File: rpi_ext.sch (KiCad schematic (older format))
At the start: 4 parts, among them J2 USB_OTG

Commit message: update pdf
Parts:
- added C11, C12, C7, C8: 10uF, symbol C_Small
- added C2: 47uF, symbol C_Small
- added C21, C22: NF, symbol C_Small
- added C6: 100nF, symbol C_Small
- added L1, L2: SRN4018-4R7M, symbol L_Small
- added PP2, PP3, PP5, PP6, PP8: TEST_1P, symbol TEST_1P
- added R2: 100K/1%, symbol R_Small
- added R22, R23: 0R/1%, symbol R_Small
- added R24, R25: 0R, symbol R_Small
- added U?: PAM2306AYPKE, symbol PAM2306AYPKE
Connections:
- net at J2.1 (VCC): now also F1.1, PP1.1
- net GND: now reaches J2.5 (GND)
- net GND: now also J2.6 (shield), C11.2, C12.2, C2.2, C6.2, C7.2, C8.2, PP5.1, PP8.1, R24.2, R25.2, U?.13 (PAD), U?.3 (GND), U?.9 (GND)
- net +5V: now reaches F1.2
- net +5V: now also C2.1, C7.1, C8.1, PP3.1, R2.1, U?.1 (VIN2), U?.6 (EN1), U?.7 (VIN1)
- new net: C22.2, R23.2, R24.1, U?.10 (FB2)
- new net: C6.1, R2.2, U?.12 (EN2)
- new net: L2.1, U?.2 (LX2)
- new net: C21.2, R22.2, R25.1, U?.4 (FB1)
- new net: L1.1, U?.8 (LX1)
- new net +1V8: C12.1, C22.1, L2.2, PP6.1, R23.1
- new net +3V3: C11.1, C21.1, L1.2, PP2.1, R22.1
- no-connect marks 0 -> 5
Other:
- moved on the sheet: PP1

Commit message: update pdf
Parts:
- added C1, C10, C3: 47uF, symbol C_Small
- added C4: 1uF, symbol C_Small
- added C5: 4.7uF, symbol C_Small
- added C9: 100nF, symbol C_Small
- added D1: RED, symbol Led_Small
- added PP4, PP7: TEST_1P, symbol TEST_1P
- added R1, R4, R5, R6: 0R, symbol R_Small
- added R3: 470R/1%, symbol R_Small
- added U2: AP7115-25SEG, symbol AP7115-25SEG
- gave numbers to parts that had none: 1
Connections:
- net labels added: CM_1V8, CM_3V3, CM_VBAT, CM_VDAC, DAC_2V5, GPIO0, GPIO0-27_VREF, GPIO1, GPIO10, GPIO11, GPIO12, GPIO13, GPIO14, GPIO15, GPIO16, GPIO17, GPIO18, GPIO19, GPIO2, GPIO20, GPIO21, GPIO22, GPIO23, GPIO24, GPIO25, GPIO26, GPIO27, GPIO28-45_VREF, GPIO3, GPIO4, GPIO5, GPIO6, GPIO7, GPIO8, GPIO9
- wire segments 50 -> 258
- no-connect marks 5 -> 15
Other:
- moved on the sheet: J?

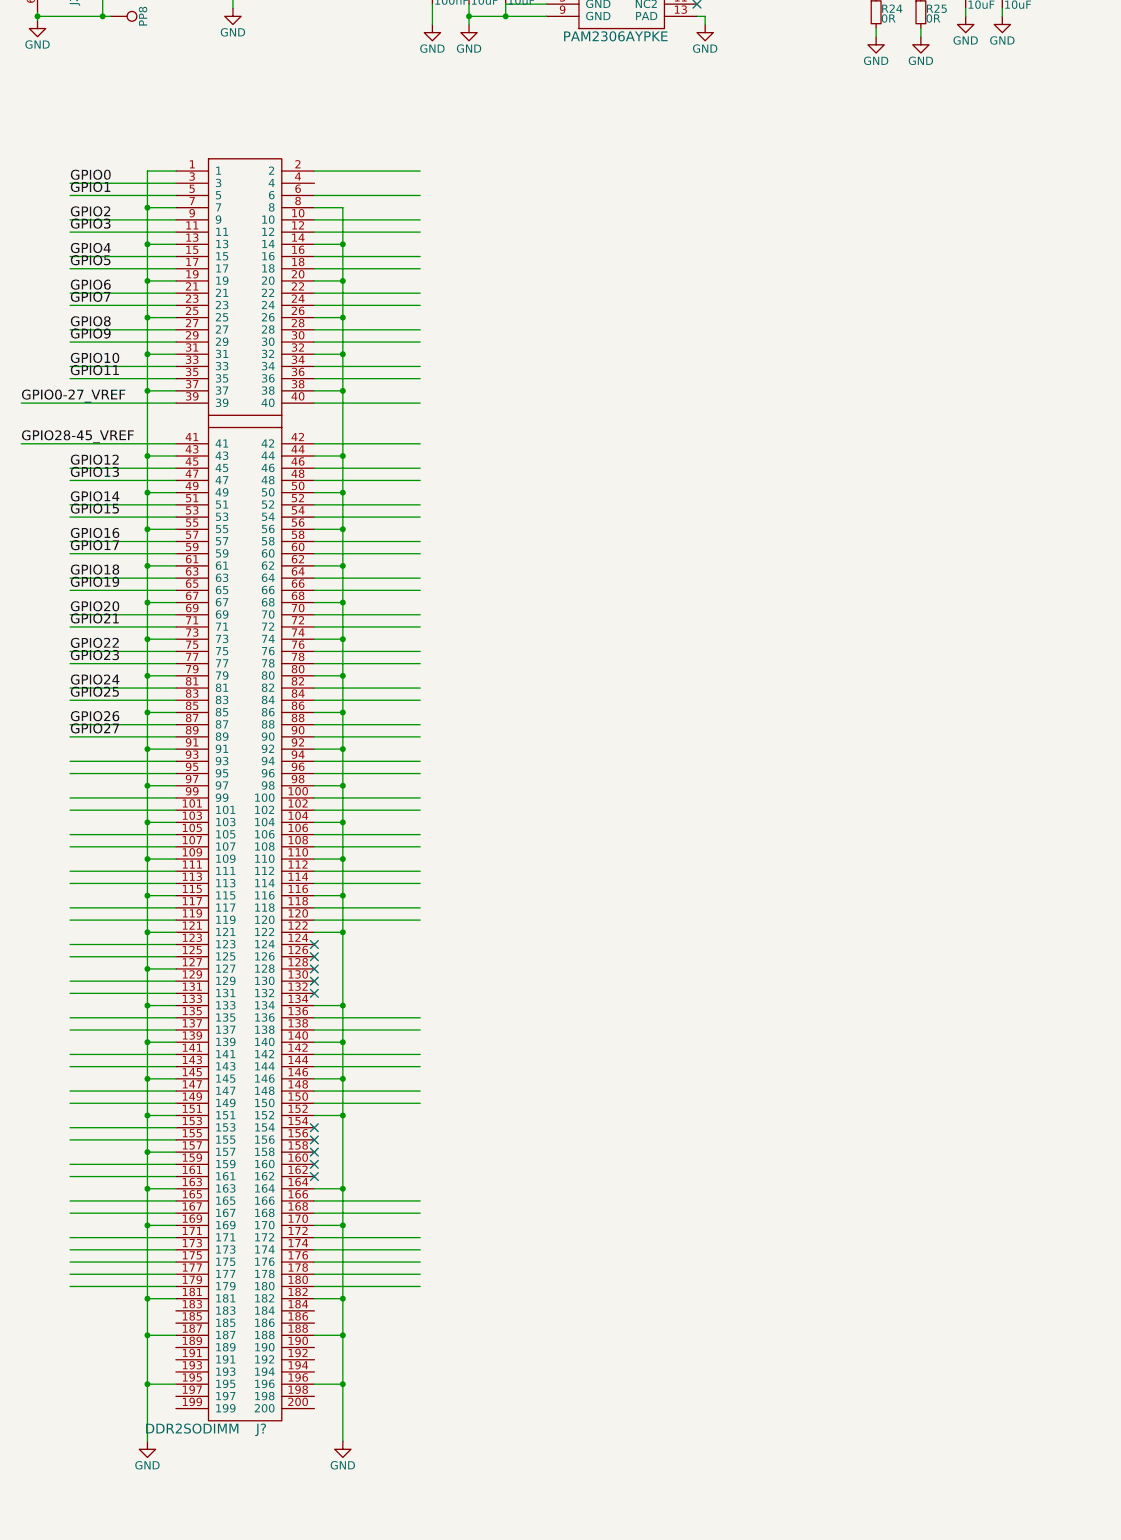
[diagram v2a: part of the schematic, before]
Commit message: update SODIMM
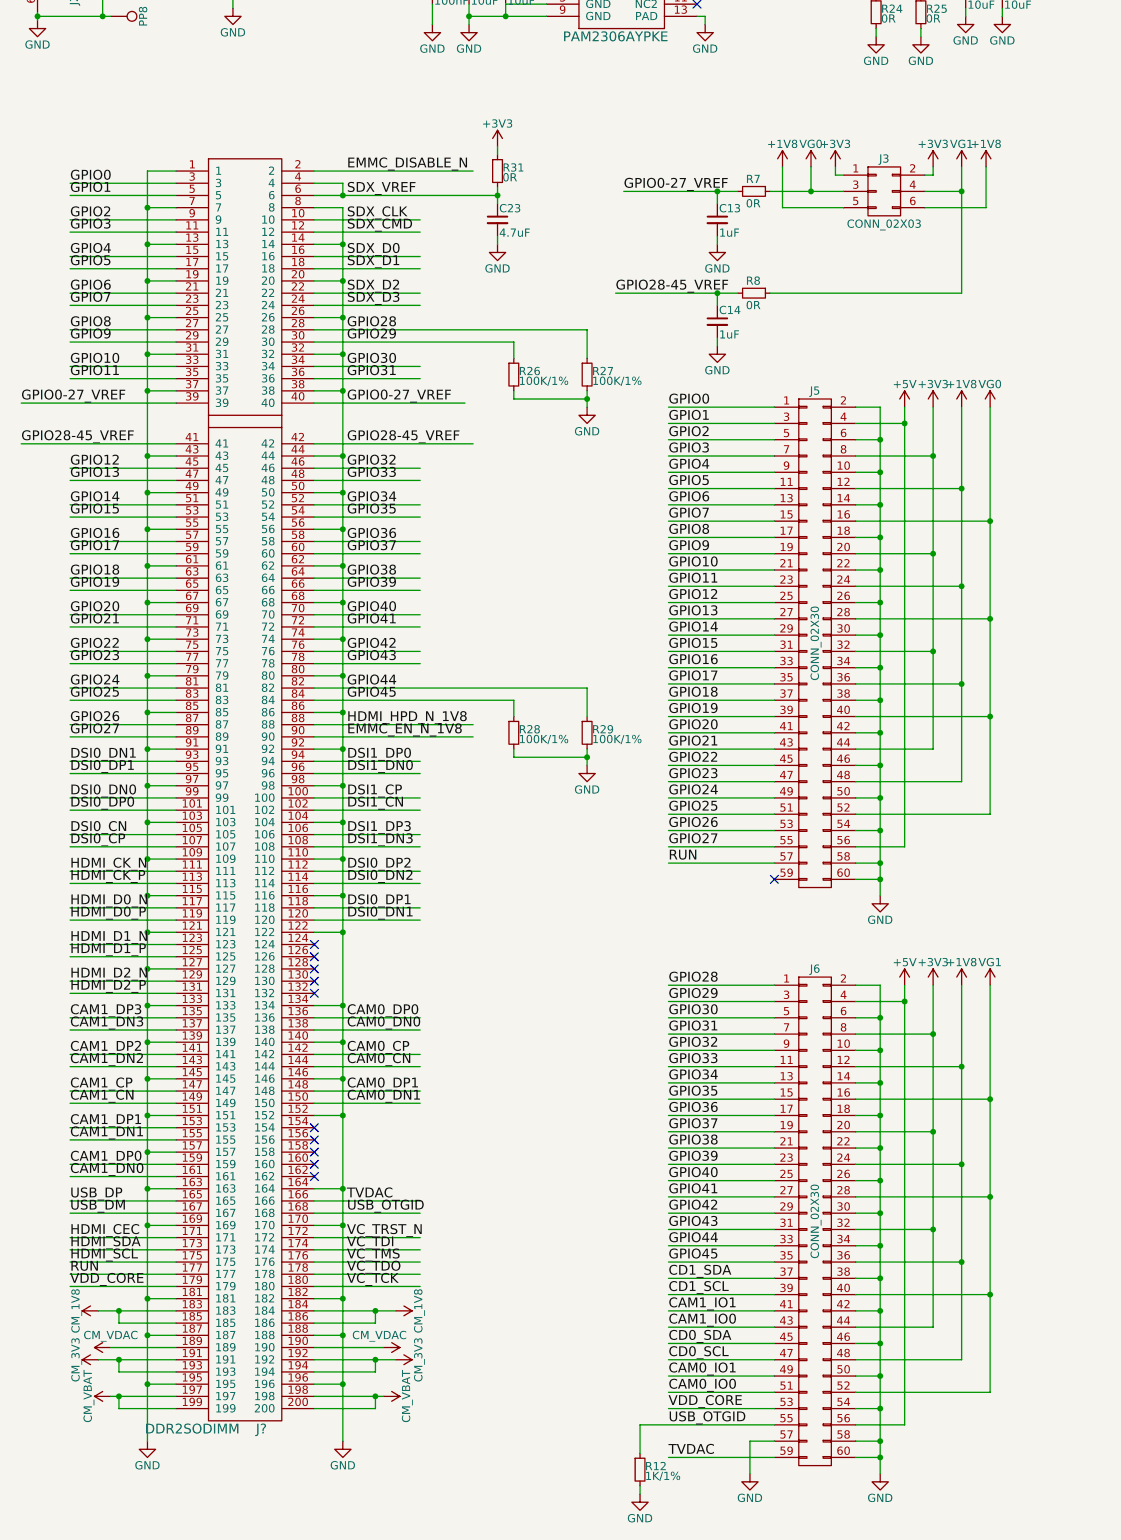
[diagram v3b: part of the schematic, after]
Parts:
- added C13, C14: 1uF, symbol C_Small
- added C23: 4.7uF, symbol C_Small
- added J3: CONN_02X03, symbol CONN_02X03
- added J5, J6: CONN_02X30, symbol CONN_02X30
- added R12: 1K/1%, symbol R_Small
- added R26, R27, R28, R29: 100K/1%, symbol R_Small
- added R31, R7, R8: 0R, symbol R_Small
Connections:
- net labels added: CAM0_CN, CAM0_CP, CAM0_DN0, CAM0_DN1, CAM0_DP0, CAM0_DP1, CAM0_IO0, CAM0_IO1, CAM1_CN, CAM1_CP, CAM1_DN0, CAM1_DN1, CAM1_DN2, CAM1_DN3, CAM1_DP0, CAM1_DP1, CAM1_DP2, CAM1_DP3, CAM1_IO0, CAM1_IO1, CD0_SCL, CD0_SDA, CD1_SCL, CD1_SDA, DSI0_CN, DSI0_CP, DSI0_DN0, DSI0_DN1, DSI0_DN2, DSI0_DP0, DSI0_DP1, DSI0_DP2, DSI1_CN, DSI1_CP, DSI1_DN0, DSI1_DN3, DSI1_DP0, DSI1_DP3, EMMC_DISABLE_N, EMMC_EN_N_1V8, GPIO28, GPIO29, GPIO30, GPIO31, GPIO32, GPIO33, GPIO34, GPIO35, GPIO36, GPIO37, GPIO38, GPIO39, GPIO40, GPIO41, GPIO42, GPIO43, GPIO44, GPIO45, HDMI_CEC, HDMI_CK_N, HDMI_CK_P, HDMI_D0_N, HDMI_D0_P, HDMI_D1_N, HDMI_D1_P, HDMI_D2_N, HDMI_D2_P, HDMI_HPD_N_1V8, HDMI_SCL, HDMI_SDA, RUN, SDX_CLK, SDX_CMD, SDX_D0, SDX_D1, SDX_D2, SDX_D3, SDX_VREF, TVDAC, USB_DM, USB_DP, USB_OTGID, VC_TCK, VC_TDI, VC_TDO, VC_TMS, VC_TRST_N, VDD_CORE, VG0, VG1
- wire segments 258 -> 444
- no-connect marks 15 -> 16

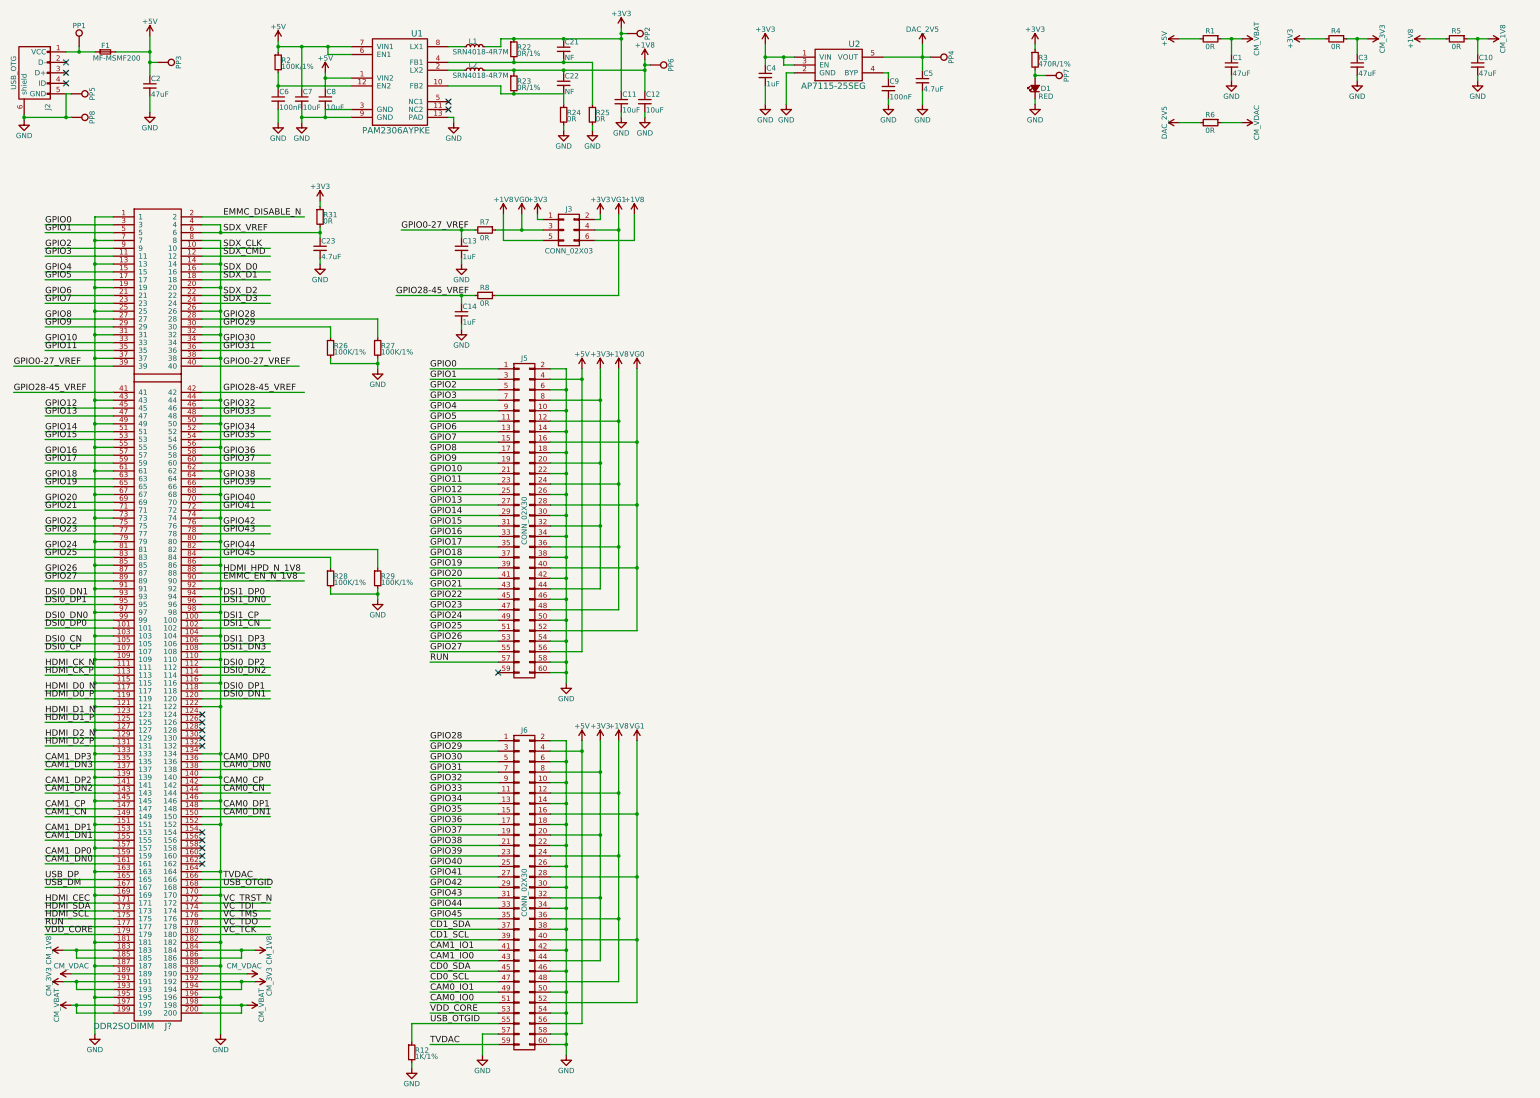
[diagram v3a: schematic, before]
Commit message: update CAM0 DISP
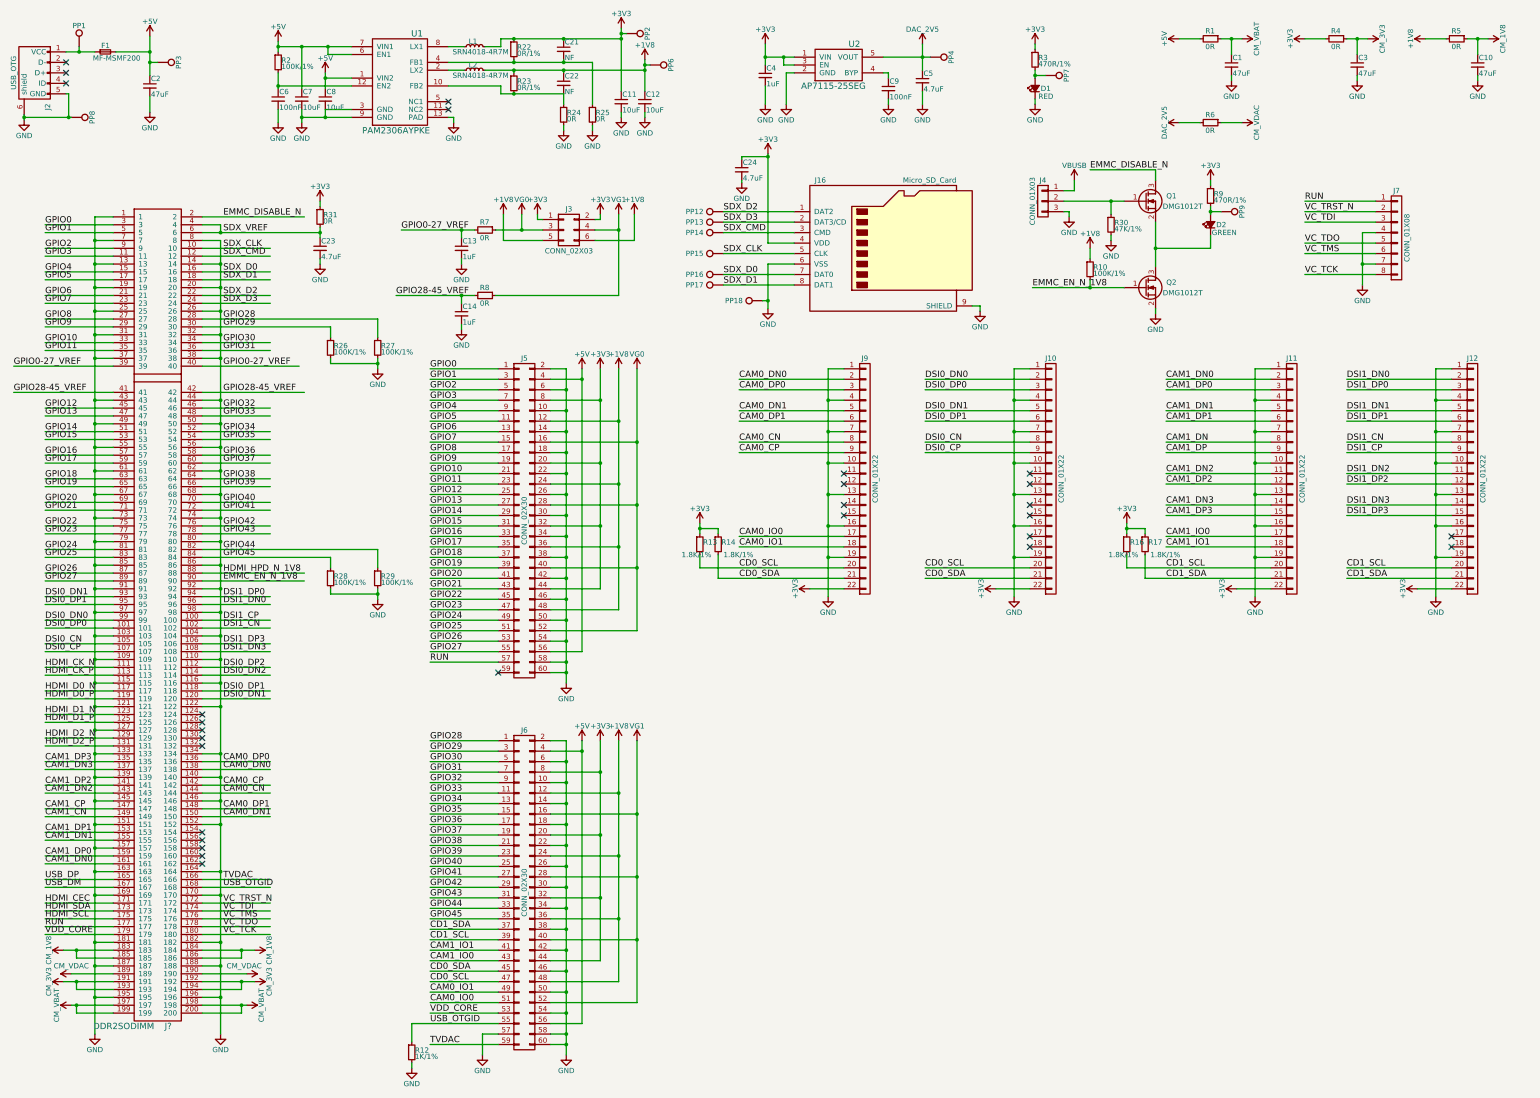
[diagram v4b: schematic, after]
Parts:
- removed PP5: TEST_1P, symbol TEST_1P
- added C24: 4.7uF, symbol C_Small
- added D2: GREEN, symbol Led_Small
- added J10, J11, J12, J9: CONN_01X22, symbol CONN_01X22
- added J16: Micro_SD_Card, symbol Micro_SD_Card
- added J4: CONN_01X03, symbol CONN_01X03
- added J7: CONN_01X08, symbol CONN_01X08
- added PP12, PP13, PP14, PP15, PP16, PP17, PP18, PP9: TEST_1P, symbol TEST_1P
- added Q1, Q2: DMG1012T, symbol Q_NMOS_GSD
- added R10: 100K/1%, symbol R_Small
- added R13, R14, R16, R17: 1.8K/1%, symbol R_Small
- added R30: 47K/1%, symbol R_Small
- added R9: 470R/1%, symbol R_Small
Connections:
- net labels added: CAM1_DN, CAM1_DP, DSI1_DN1, DSI1_DN2, DSI1_DP1, DSI1_DP2, VBUSB
- wire segments 444 -> 578
- no-connect marks 16 -> 28

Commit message: update USB
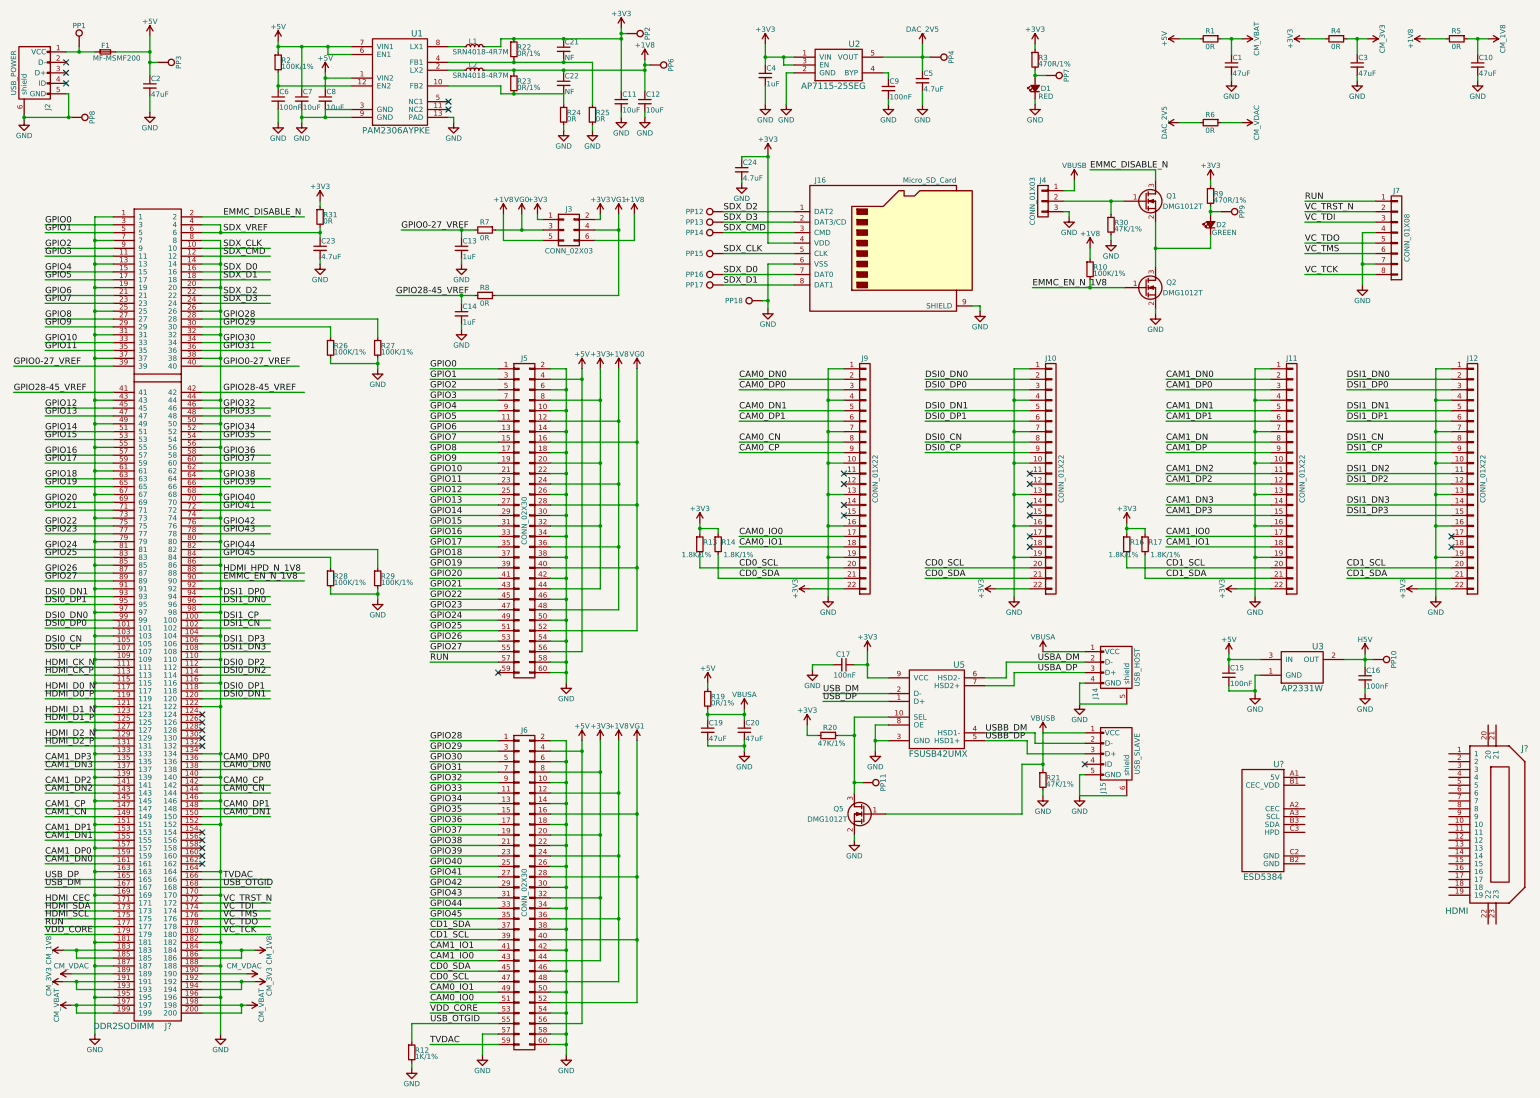
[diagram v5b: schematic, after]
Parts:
- added C15, C16, C17: 100nF, symbol C_Small
- added C19, C20: 47uF, symbol C_Small
- added J14: USB_HOST, symbol USB_A
- added J15: USB_SLAVE, symbol USB_OTG
- added J?: HDMI, symbol HDMI
- added PP10, PP11: TEST_1P, symbol TEST_1P
- added Q5: DMG1012T, symbol Q_NMOS_GSD
- added R19: 0R/1%, symbol R_Small
- added R20, R21: 47K/1%, symbol R_Small
- added U3: AP2331W, symbol AP2331W
- added U5: FSUSB42UMX, symbol FSUSB42UMX
- added U?: ESD5384, symbol ESD5384
- J2: value USB_OTG -> USB_POWER
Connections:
- net labels added: H5V, USBA_DM, USBA_DP, USBB_DM, USBB_DP, VBUSA
- wire segments 578 -> 636
- no-connect marks 28 -> 29
